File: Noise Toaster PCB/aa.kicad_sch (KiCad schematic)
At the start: 14 parts, among them U3 LM386, X12 Conn_01x01_Pin

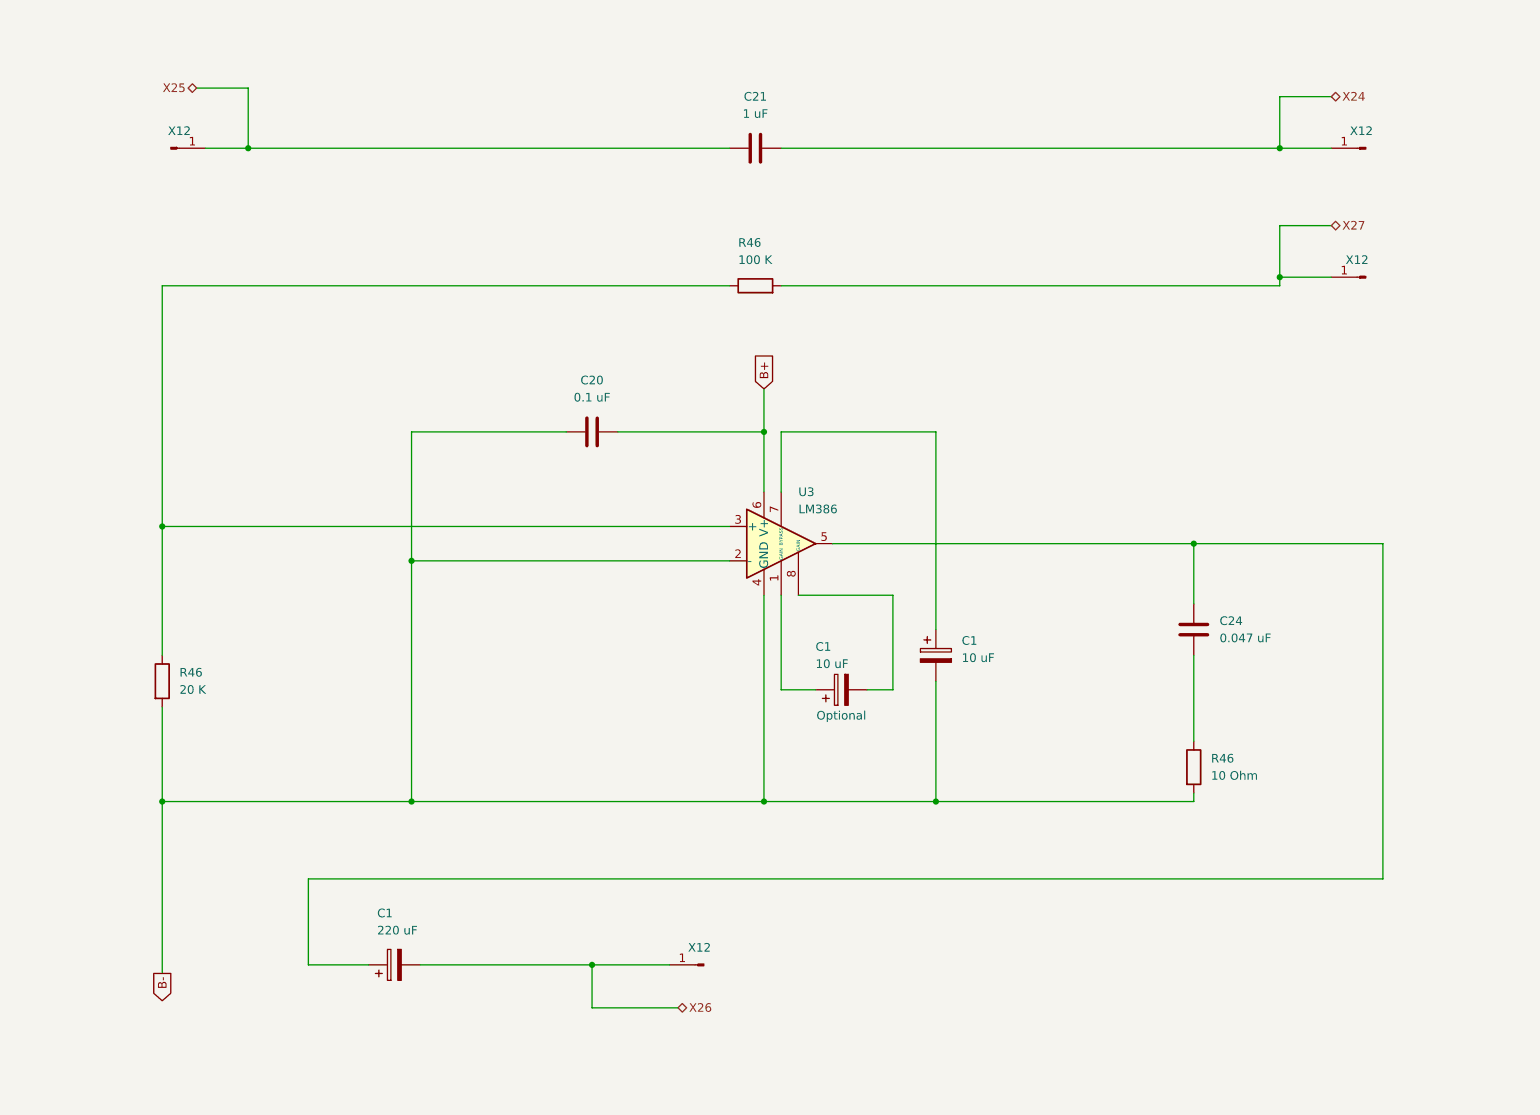
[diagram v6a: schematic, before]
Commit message: changed header pins to groups
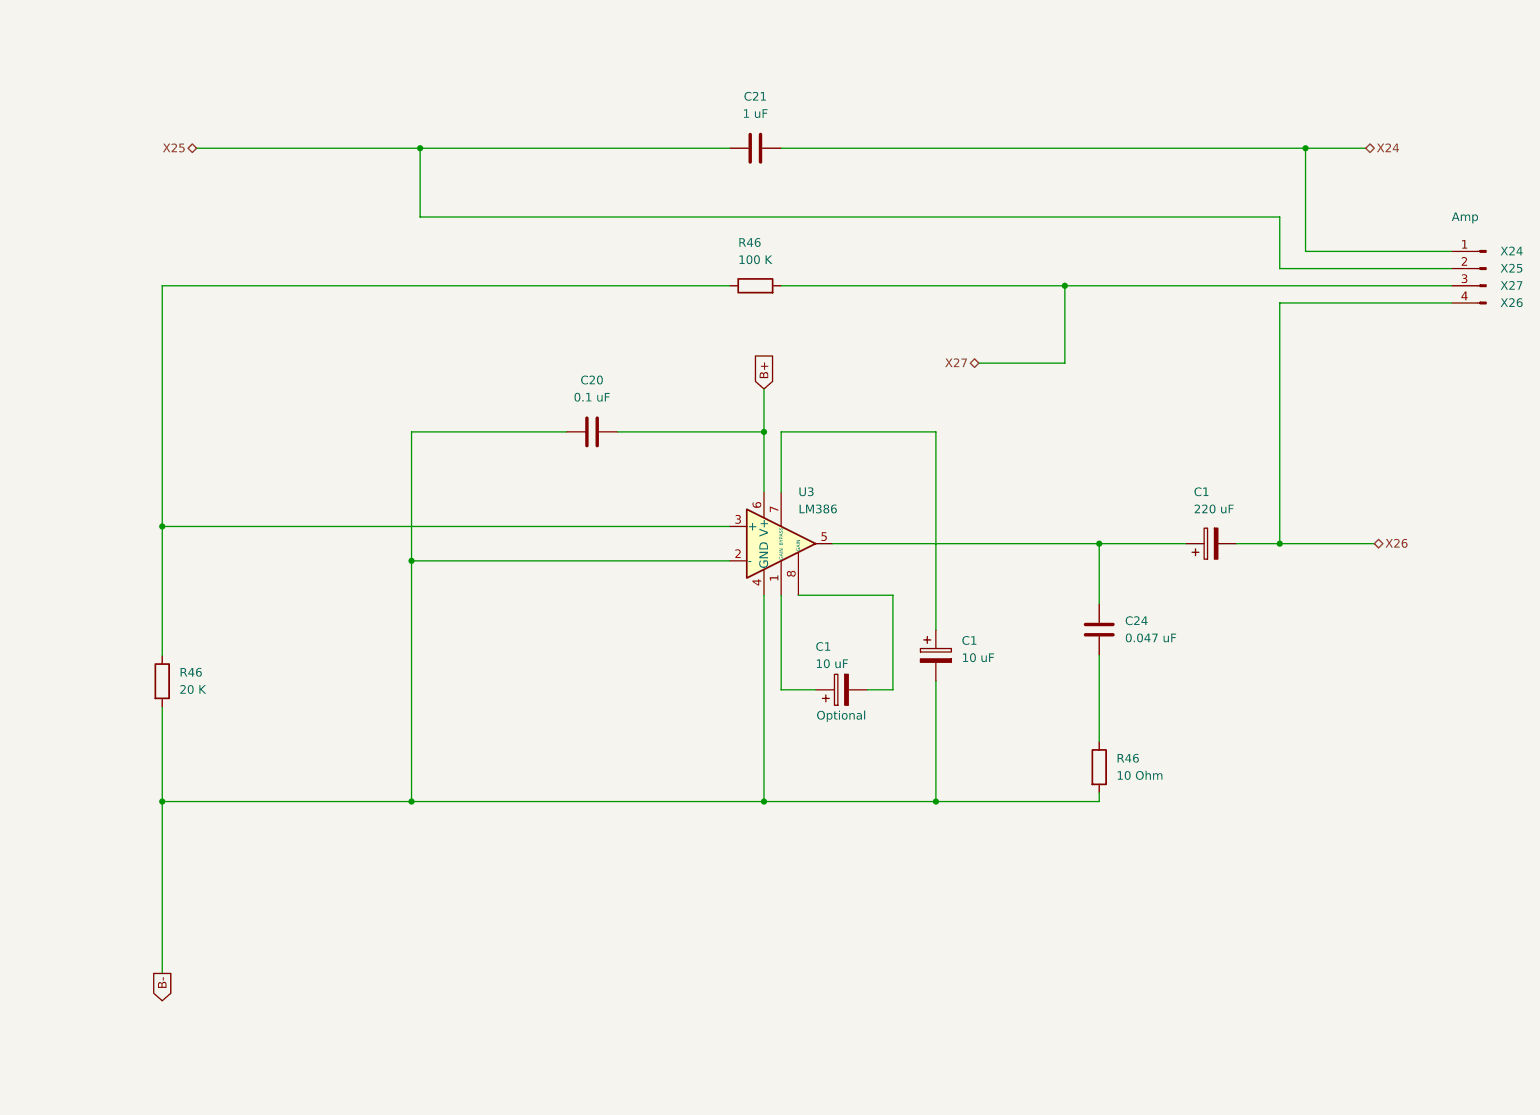
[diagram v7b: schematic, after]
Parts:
- removed X12 (x4): Conn_01x01_Pin, Connector_PinHeader_1.00mm:PinHeader_1x01_P1.00mm_Vertical, symbol Connector:Conn_01x01_Pin
- added J9: Amp, Connector_PinHeader_2.00mm:PinHeader_1x04_P2.00mm_Vertical, symbol Connector:Conn_01x04_Pin
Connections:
- net X24: now also J9.1 (Pin_1)
- net X25: now also J9.2 (Pin_2)
- net X26: now also J9.4 (Pin_4)
- net X27: now also J9.3 (Pin_3)
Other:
- moved on the sheet: C1, C24, R46
